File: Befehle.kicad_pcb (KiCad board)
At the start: 2 copper layers, 100 x 160 mm, 62 parts, among them J1 2PinTerminalBlocktg, J2 2PinTerminalBlocktg, J3 3PinTerminalBlocktg, J4 2PinTerminalBlocktg, J5 2PinTerminalBlocktg, P1 CONN_02X10, P2 CONN_02X10, U1 74LS14, U2 74540, U3 7400, U4 74HCT02, U5 74LS541, U6 74LS373, U7 74LS139, U8 74LS540

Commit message: Befehle: vor Umbau der Diodenmatrix im Schalplan
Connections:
- net Net-(P2-Pad2) renamed /AB0
- net Net-(P2-Pad3) renamed /AB1
- net Net-(P2-Pad4) renamed /AB2
- net Net-(P2-Pad5) renamed /AB3
- net Net-(P2-Pad6) renamed /AB4
- net Net-(P2-Pad7) renamed /AB5
- net Net-(P2-Pad8) renamed /AB6
- net Net-(P2-Pad9) renamed /AB7
- U1 pad 8: (no net) -> Net-(U1-Pad8)

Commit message: Befehle: Schaltplan bearbeitet
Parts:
- removed G***: LOGO, allBonsaiFootprintsLibs:agi5
- added C3: 100n, Capacitor_THT:C_Disc_D10.0mm_W2.5mm_P5.00mm, F.Cu at (129.0, 126.1)
- added C4: 100n, Capacitor_THT:C_Disc_D10.0mm_W2.5mm_P5.00mm, F.Cu at (129.0, 113.9)
- added C5: 100n, Capacitor_THT:C_Disc_D10.0mm_W2.5mm_P5.00mm, F.Cu at (129.0, 118.0)
- added C6: 100n, Capacitor_THT:C_Disc_D10.0mm_W2.5mm_P5.00mm, F.Cu at (140.6, 113.9)
- added C7: 100n, Capacitor_THT:C_Disc_D10.0mm_W2.5mm_P5.00mm, F.Cu at (129.0, 122.0)
- added C8: 100n, Capacitor_THT:C_Disc_D10.0mm_W2.5mm_P5.00mm, F.Cu at (140.6, 118.0)
- added C9: CP, Capacitor_THT:CP_Radial_D8.0mm_P2.50mm, F.Cu at (36.3, 11.1)
- added D23: bonsai_Led_Small_Platzhalter, bonsai:LED_Diodenmatrix_Platzhalter, F.Cu at (144.3, 121.8)
- added D24: bonsai_Led_Small_Platzhalter, bonsai:LED_Diodenmatrix_Platzhalter, F.Cu at (138.8, 125.5)
- added D25: bonsai_Led_Small_Platzhalter, bonsai:LED_Diodenmatrix_Platzhalter, F.Cu at (138.8, 121.8)
- added D26: bonsai_Led_Small_Platzhalter, bonsai:LED_Diodenmatrix_Platzhalter, F.Cu at (138.8, 129.1)
- added D27: bonsai_Led_Small_Platzhalter, bonsai:LED_Diodenmatrix_Platzhalter, F.Cu at (149.9, 123.3)
- added D28: bonsai_Led_Small_Platzhalter, bonsai:LED_Diodenmatrix_Platzhalter, F.Cu at (144.3, 125.5)
- added D29: bonsai_Led_Small_Platzhalter, bonsai:LED_Diodenmatrix_Platzhalter, F.Cu at (144.3, 129.1)
- added D30: bonsai_Led_Small_Platzhalter, bonsai:LED_Diodenmatrix_Platzhalter, F.Cu at (149.9, 126.9)
- added D31: bonsai_Led_Small_Platzhalter, bonsai:LED_Diodenmatrix_Platzhalter, F.Cu at (155.4, 123.3)
- added D32: bonsai_Led_Small_Platzhalter, bonsai:LED_Diodenmatrix_Platzhalter, F.Cu at (155.4, 126.9)
- C1, C2: footprint Capacitors_ThroughHole:C_Disc_D10.0mm_W2.5mm_P5.00mm -> Capacitor_THT:C_Disc_D10.0mm_W2.5mm_P5.00mm
- D11, D12, D15, D16, D19, D20: footprint allBonsaiFootprintsLibs:Diode_D1.8mm_W3.3mm_H2.4mmBonsai -> bonsai:LED_Diodenmatrix
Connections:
- D11 pad 1: 3 -> Net-(D11-Pad1)
- D11 pad 2: Net-(D11-Pad2) -> 3
- D12 pad 1: 3 -> Net-(D12-Pad1)
- D12 pad 2: Net-(D12-Pad2) -> 3
- D15 pad 1: 2 -> Net-(D11-Pad1)
- D15 pad 2: Net-(D11-Pad2) -> 2
- D16 pad 1: 2 -> Net-(D16-Pad1)
- D16 pad 2: Net-(D16-Pad2) -> 2
- D19 pad 1: 1 -> Net-(D19-Pad1)
- D19 pad 2: Net-(D19-Pad2) -> 1
- D20 pad 1: 0 -> Net-(D19-Pad1)
- D20 pad 2: Net-(D19-Pad2) -> 0
- U2 pad 1: GND -> Net-(U2-Pad1)
- U7 pad 4: Net-(D11-Pad2) -> Net-(D11-Pad1)
- U7 pad 5: Net-(D12-Pad2) -> Net-(D12-Pad1)
- U7 pad 6: Net-(D16-Pad2) -> Net-(D16-Pad1)
- U7 pad 7: Net-(D19-Pad2) -> Net-(D19-Pad1)
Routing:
- net Net-(D19-Pad2): track 47.8 -> 0.00 mm, vias 2 -> 0
- net Net-(D19-Pad1): track 0.00 -> 47.8 mm, vias 0 -> 2
- net Net-(D16-Pad2): track 46.1 -> 0.00 mm, vias 2 -> 0
- net Net-(D16-Pad1): track 0.00 -> 46.1 mm, vias 0 -> 2
- net Net-(D12-Pad2): track 42.4 -> 0.00 mm, vias 2 -> 0
- net Net-(D12-Pad1): track 0.00 -> 42.4 mm, vias 0 -> 2
- net Net-(D11-Pad2): track 38.2 -> 0.00 mm, vias 2 -> 0
- net Net-(D11-Pad1): track 0.00 -> 38.2 mm, vias 0 -> 2

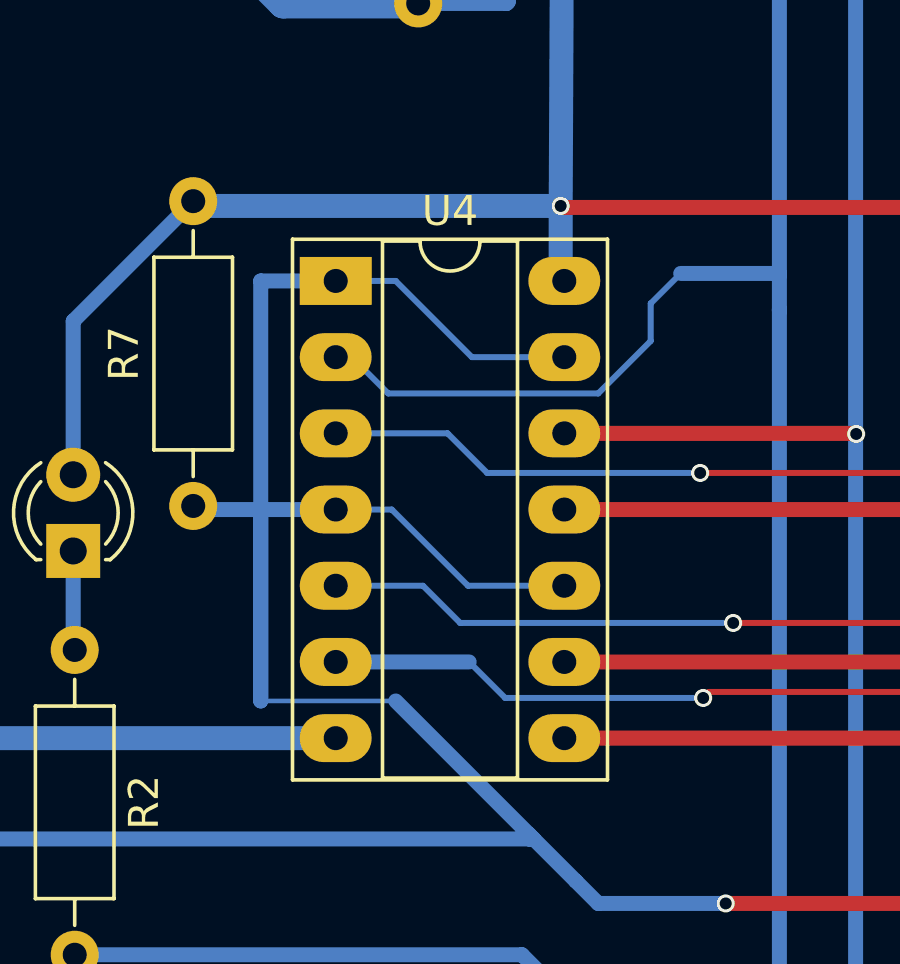
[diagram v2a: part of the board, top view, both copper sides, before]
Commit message: Befehle: Schaltplan geändert
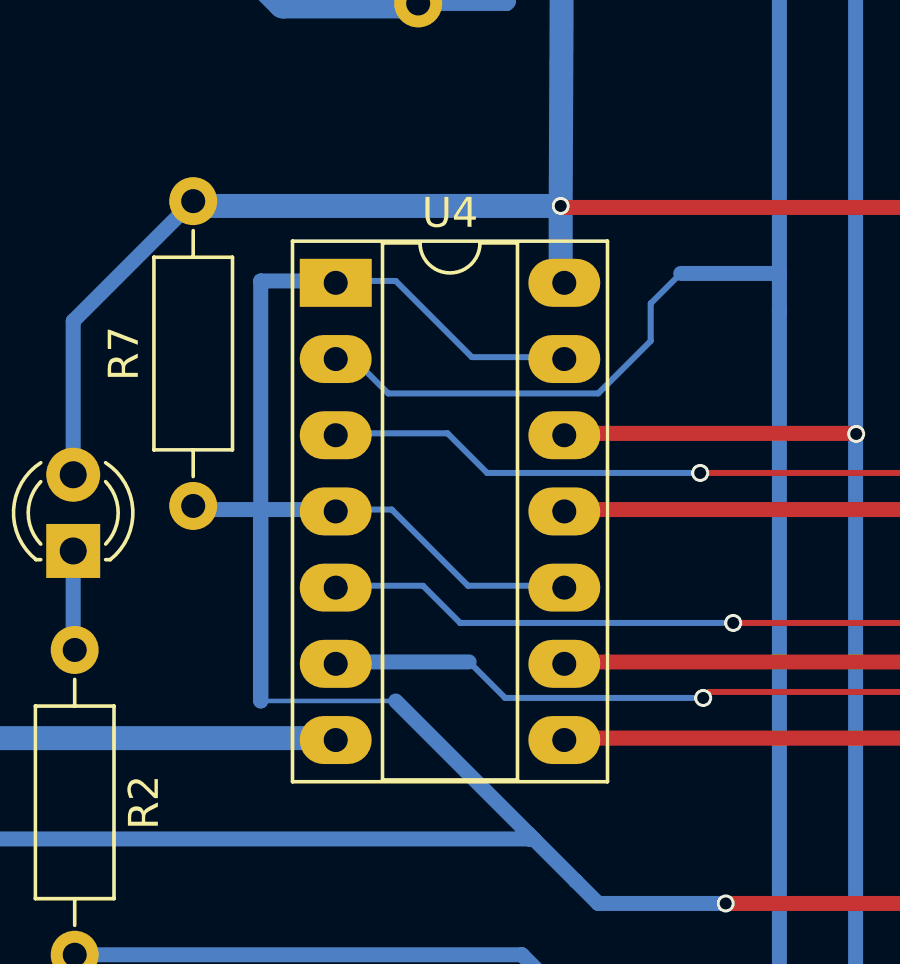
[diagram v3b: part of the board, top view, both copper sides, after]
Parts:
- U4: footprint allBonsaiFootprintsLibs:DIP-14_W7.62mm_Socket_LongPadstg -> Package_DIP:DIP-14_W7.62mm_Socket_LongPads
- moved U4 0.06 mm to (33.8, 117.1)
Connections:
- P2 pad 2: /AB0 -> /AB7
- P2 pad 3: /AB1 -> /AB6
- P2 pad 4: /AB2 -> /AB5
- P2 pad 5: /AB3 -> /AB4
- P2 pad 6: /AB4 -> /AB3
- P2 pad 7: /AB5 -> /AB2
- P2 pad 8: /AB6 -> /AB1
- P2 pad 9: /AB7 -> /AB0
- U2 pad 1: Net-(U2-Pad1) -> GND
- U5 pad 11: /AB0 -> /AB7
- U5 pad 12: /AB1 -> /AB6
- U5 pad 13: /AB2 -> /AB5
- U5 pad 14: /AB3 -> /AB4
- U5 pad 15: /AB4 -> /AB3
- U5 pad 16: /AB5 -> /AB2
- U5 pad 17: /AB6 -> /AB1
- U5 pad 18: /AB7 -> /AB0
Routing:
- net /AB7: track 34.0 -> 61.4 mm
- net /AB0: track 61.4 -> 34.0 mm
- net /AB6: track 37.3 -> 58.0 mm
- net /AB1: track 58.0 -> 37.3 mm
- net /AB5: track 41.2 -> 53.3 mm
- net /AB2: track 53.3 -> 41.2 mm
- net /AB4: track 45.1 -> 48.9 mm
- net /AB3: track 48.9 -> 45.1 mm

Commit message: Steuerwerk und Befehle bearbeitet
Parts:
- removed the C1 at (76.0, 60.0)
- removed the D17 at (99.0, 164.8)
- removed the D19 at (98.9, 125.4)
- removed the D30 at (149.9, 126.9)
- removed the D31 at (155.4, 123.3)
- removed the D32 at (155.4, 126.9)
- removed the D4 at (89.0, 164.8)
- removed the D7 at (94.0, 164.8)
- removed P1, P2: CONN_02X10, allBonsaiFootprintsLibs:Pin_Header_Straight_2x10_Pitch2.00mmBonsai.pretty
- removed the REF** at (116.3, 180.1)
- removed the U5 at (46.0, 67.0)
- added C10: 100n, Capacitor_THT:C_Disc_D10.0mm_W2.5mm_P5.00mm, F.Cu at (23.6, 66.4)
- added C2: 100n, Capacitor_THT:C_Disc_D10.0mm_W2.5mm_P5.00mm, F.Cu at (45.2, 58.8)
- added D11: bonsai_Led_Small_Platzhalter, bonsai:LED_Diodenmatrix_Platzhalter, F.Cu at (139.9, 137.5)
- added D13: Led_Small, bonsai:LED_Diodenmatrix, F.Cu at (132.3, 141.3)
- added D14: bonsai_Led_Small_Platzhalter, bonsai:LED_Diodenmatrix_Platzhalter, F.Cu at (136.1, 141.3)
- added D15: bonsai_Led_Small_Platzhalter, bonsai:LED_Diodenmatrix_Platzhalter, F.Cu at (139.9, 141.3)
- added D16: bonsai_Led_Small_Platzhalter, bonsai:LED_Diodenmatrix_Platzhalter, F.Cu at (143.7, 141.3)
- added D18: bonsai_Led_Small_Platzhalter, bonsai:LED_Diodenmatrix_Platzhalter, F.Cu at (132.3, 145.1)
- added D22: bonsai_Led_Small_Platzhalter, bonsai:LED_Diodenmatrix_Platzhalter, F.Cu at (132.3, 148.9)
- added J6: Conn_01x03, Connector_Molex:Molex_KK-254_AE-6410-03A_1x03_P2.54mm_Vertical, F.Cu at (2.33, 76.9)
- added REF**: EuroBoard160mmX100mm_holes_keepout, bonsai:EuroBoard160mmX100mm_holes_keepout, F.Cu at (114.2, 182.4)
- added U2: 74LS541, Package_DIP:DIP-20_W7.62mm_LongPads, F.Cu at (49.0, 65.1)
- added U8: 7408, Package_DIP:DIP-14_W7.62mm_Socket_LongPads, F.Cu at (21.7, 124.2)
- D1: renamed from D5; footprint LEDs:LED_D3.0mm -> LED_THT:LED_D3.0mm
- D12, D20: value Led_Small -> bonsai_Led_Small_Platzhalter; footprint bonsai:LED_Diodenmatrix -> bonsai:LED_Diodenmatrix_Platzhalter
- D17: renamed from D2; footprint LEDs:LED_D3.0mm -> LED_THT:LED_D3.0mm
- D2: renamed from D6; footprint LEDs:LED_D3.0mm -> LED_THT:LED_D3.0mm
- D21: value LED -> bonsai_Led_Small_Platzhalter; footprint LEDs:LED_D3.0mm -> bonsai:LED_Diodenmatrix_Platzhalter
- D24, D25: value bonsai_Led_Small_Platzhalter -> Led_Small; footprint bonsai:LED_Diodenmatrix_Platzhalter -> bonsai:LED_Diodenmatrix
- D26, D27, D28, D29: value bonsai_Led_Small_Platzhalter -> LED; footprint bonsai:LED_Diodenmatrix_Platzhalter -> LED_THT:LED_D3.0mm
- D3: renamed from D8; footprint LEDs:LED_D3.0mm -> LED_THT:LED_D3.0mm
- D30: renamed from D3; footprint LEDs:LED_D3.0mm -> LED_THT:LED_D3.0mm
- D31: renamed from D1; footprint LEDs:LED_D3.0mm -> LED_THT:LED_D3.0mm
- D32: renamed from D22; footprint Diodes_ThroughHole:D_DO-41_SOD81_P10.16mm_Horizontal -> Diode_THT:D_A-405_P10.16mm_Horizontal
- D4: renamed from D9; footprint LEDs:LED_D3.0mm -> LED_THT:LED_D3.0mm
- D5: renamed from D10; footprint LEDs:LED_D3.0mm -> LED_THT:LED_D3.0mm
- D6: renamed from D13; footprint LEDs:LED_D3.0mm -> LED_THT:LED_D3.0mm
- D7: renamed from D14; footprint LEDs:LED_D3.0mm -> LED_THT:LED_D3.0mm
- D8: renamed from D18; footprint LEDs:LED_D3.0mm -> LED_THT:LED_D3.0mm
- J1, J4: value 2PinTerminalBlocktg -> Conn_02x10_Odd_Even; footprint 2PinTerminalBlocktg -> Connector_PinHeader_2.54mm:PinHeader_2x10_P2.54mm_Vertical
- J2, J5: value 2PinTerminalBlocktg -> Conn_01x02; footprint 2PinTerminalBlocktg -> Connector_Molex:Molex_KK-254_AE-6410-02A_1x02_P2.54mm_Vertical
- J3: value 3PinTerminalBlocktg -> Conn_01x04; footprint 3PinTerminalBlocktg -> Connector_Molex:Molex_KK-254_AE-6410-04A_1x04_P2.54mm_Vertical
- R1: renamed from R10; footprint Resistors_ThroughHole:R_Axial_DIN0207_L6.3mm_D2.5mm_P10.16mm_Horizontal -> Resistor_THT:R_Axial_DIN0207_L6.3mm_D2.5mm_P10.16mm_Horizontal
- R10: renamed from R5; footprint Resistors_ThroughHole:R_Axial_DIN0207_L6.3mm_D2.5mm_P10.16mm_Horizontal -> Resistor_THT:R_Axial_DIN0207_L6.3mm_D2.5mm_P10.16mm_Horizontal
- R11: renamed from R4; footprint Resistors_ThroughHole:R_Axial_DIN0207_L6.3mm_D2.5mm_P10.16mm_Horizontal -> Resistor_THT:R_Axial_DIN0207_L6.3mm_D2.5mm_P10.16mm_Horizontal
- R12: renamed from R9; footprint Resistors_ThroughHole:R_Axial_DIN0207_L6.3mm_D2.5mm_P10.16mm_Horizontal -> Resistor_THT:R_Axial_DIN0207_L6.3mm_D2.5mm_P10.16mm_Horizontal
- R13: renamed from R12; footprint Resistors_ThroughHole:R_Axial_DIN0207_L6.3mm_D2.5mm_P10.16mm_Horizontal -> Resistor_THT:R_Axial_DIN0207_L6.3mm_D2.5mm_P10.16mm_Horizontal
- R14: renamed from R20; footprint Resistors_ThroughHole:R_Axial_DIN0207_L6.3mm_D2.5mm_P10.16mm_Horizontal -> Resistor_THT:R_Axial_DIN0207_L6.3mm_D2.5mm_P10.16mm_Horizontal
- R15: renamed from R24; footprint Resistors_ThroughHole:R_Axial_DIN0207_L6.3mm_D2.5mm_P10.16mm_Horizontal -> Resistor_THT:R_Axial_DIN0207_L6.3mm_D2.5mm_P10.16mm_Horizontal
- R16: renamed from R8; footprint Resistors_ThroughHole:R_Axial_DIN0207_L6.3mm_D2.5mm_P10.16mm_Horizontal -> Resistor_THT:R_Axial_DIN0207_L6.3mm_D2.5mm_P10.16mm_Horizontal
- R17: renamed from R2; footprint Resistors_ThroughHole:R_Axial_DIN0207_L6.3mm_D2.5mm_P10.16mm_Horizontal -> Resistor_THT:R_Axial_DIN0207_L6.3mm_D2.5mm_P10.16mm_Horizontal
- R18: renamed from R3; footprint Resistors_ThroughHole:R_Axial_DIN0207_L6.3mm_D2.5mm_P10.16mm_Horizontal -> Resistor_THT:R_Axial_DIN0207_L6.3mm_D2.5mm_P10.16mm_Horizontal
- R19: renamed from R6; footprint Resistors_ThroughHole:R_Axial_DIN0207_L6.3mm_D2.5mm_P10.16mm_Horizontal -> Resistor_THT:R_Axial_DIN0207_L6.3mm_D2.5mm_P10.16mm_Horizontal
- R2: renamed from R11; footprint Resistors_ThroughHole:R_Axial_DIN0207_L6.3mm_D2.5mm_P10.16mm_Horizontal -> Resistor_THT:R_Axial_DIN0207_L6.3mm_D2.5mm_P10.16mm_Horizontal
- R3: renamed from R13; footprint Resistors_ThroughHole:R_Axial_DIN0207_L6.3mm_D2.5mm_P10.16mm_Horizontal -> Resistor_THT:R_Axial_DIN0207_L6.3mm_D2.5mm_P10.16mm_Horizontal
- R4: renamed from R14; footprint Resistors_ThroughHole:R_Axial_DIN0207_L6.3mm_D2.5mm_P10.16mm_Horizontal -> Resistor_THT:R_Axial_DIN0207_L6.3mm_D2.5mm_P10.16mm_Horizontal
- R5: renamed from R15; footprint Resistors_ThroughHole:R_Axial_DIN0207_L6.3mm_D2.5mm_P10.16mm_Horizontal -> Resistor_THT:R_Axial_DIN0207_L6.3mm_D2.5mm_P10.16mm_Horizontal
- R6: renamed from R16; footprint Resistors_ThroughHole:R_Axial_DIN0207_L6.3mm_D2.5mm_P10.16mm_Horizontal -> Resistor_THT:R_Axial_DIN0207_L6.3mm_D2.5mm_P10.16mm_Horizontal
- R7: renamed from R18; footprint Resistors_ThroughHole:R_Axial_DIN0207_L6.3mm_D2.5mm_P10.16mm_Horizontal -> Resistor_THT:R_Axial_DIN0207_L6.3mm_D2.5mm_P10.16mm_Horizontal
- R8: renamed from R21; footprint Resistors_ThroughHole:R_Axial_DIN0207_L6.3mm_D2.5mm_P10.16mm_Horizontal -> Resistor_THT:R_Axial_DIN0207_L6.3mm_D2.5mm_P10.16mm_Horizontal
- R9: renamed from R1; footprint Resistors_ThroughHole:R_Axial_DIN0207_L6.3mm_D2.5mm_P10.16mm_Horizontal -> Resistor_THT:R_Axial_DIN0207_L6.3mm_D2.5mm_P10.16mm_Horizontal
- RP1: footprint Resistors_ThroughHole:R_Array_SIP5 -> Resistor_THT:R_Array_SIP5
- U1: footprint allBonsaiFootprintsLibs:DIP-14_W7.62mm_Socket_LongPadstg -> Package_DIP:DIP-14_W7.62mm_Socket_LongPads
- U3: renamed from U8; footprint allBonsaiFootprintsLibs:DIP-20_W7.62mm_Socket_LongPadstg -> Package_DIP:DIP-20_W7.62mm_LongPads
- U4: renamed from U7; footprint allBonsaiFootprintsLibs:DIP-16_W7.62mm_Socket_LongPadstg -> Package_DIP:DIP-16_W7.62mm_Socket_LongPads
- U5: renamed from U6; footprint allBonsaiFootprintsLibs:DIP-20_W7.62mm_Socket_LongPadstg -> Package_DIP:DIP-20_W7.62mm_LongPads
- U6: renamed from U2; footprint allBonsaiFootprintsLibs:DIP-20_W7.62mm_Socket_LongPadstg -> Package_DIP:DIP-20_W7.62mm_LongPads
- U7: renamed from U4; value 74HCT02 -> 7402
- U9: renamed from U3; footprint allBonsaiFootprintsLibs:DIP-14_W7.62mm_Socket_LongPadstg -> Package_DIP:DIP-14_W7.62mm_Socket_LongPads
- moved J5 159.5 mm to (34.3, 25.2), turned to 0 degrees
- moved C8 106.1 mm to (23.0, 120.4)
- moved C9 104.8 mm to (39.5, 145.8)
- moved C7 101.3 mm to (39.5, 120.4)
- moved C5 87.9 mm to (42.6, 97.5), turned to 270 degrees
- moved J3 77.7 mm to (100.8, 174.6), turned to 180 degrees
- moved D27 69.6 mm to (94.0, 164.8), turned to 270 degrees
- moved D26 61.3 mm to (89.0, 164.8), turned to 270 degrees
- moved D28 60.0 mm to (99.0, 164.8), turned to 270 degrees
- moved C6 55.3 mm to (79.5, 142.6), turned to 90 degrees
- moved D29 53.7 mm to (104.2, 164.8), turned to 270 degrees
- moved D12 52.7 mm to (143.7, 137.5), turned to 45 degrees
- moved C4 49.3 mm to (88.4, 98.1), turned to 270 degrees
- moved D19 45.5 mm to (136.1, 145.1), turned to 45 degrees
- moved D10 44.7 mm to (136.1, 137.5), turned to 45 degrees
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- renumbered C9 to C1, C2 to C3, C3 to C4, C4 to C5, C5 to C6, C6 to C7, C7 to C8, C8 to C9, D15 to D10, D16 to D19, D11 to D9
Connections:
- D10 pad 1: Net-(D11-Pad1) -> /h0
- D10 pad 2: 2 -> /v2
- D12 pad 1: Net-(D12-Pad1) -> /h0
- D12 pad 2: 3 -> /v0
- D19 pad 1: Net-(D16-Pad1) -> /h2
- D19 pad 2: 2 -> /v2
- D20 pad 1: Net-(D19-Pad1) -> /h2
- D20 pad 2: 0 -> /v1
- D21 pad 1: Net-(D21-Pad1) -> /h2
- D21 pad 2: VCC -> /v0
- D23 pad 1: 3 -> /h3
- D23 pad 2: Net-(D16-Pad1) -> /v2
- D24 pad 1: 1 -> /h3
- D24 pad 2: Net-(D11-Pad1) -> /v1
- D25 pad 1: 0 -> /h3
- D25 pad 2: Net-(D11-Pad1) -> /v0
- D26 pad 1: 2 -> Net-(D26-Pad1)
- D26 pad 2: Net-(D12-Pad1) -> VCC
- D27 pad 1: 1 -> Net-(D27-Pad1)
- D27 pad 2: Net-(D12-Pad1) -> VCC
- D28 pad 1: 0 -> Net-(D28-Pad1)
- D28 pad 2: Net-(D12-Pad1) -> VCC
- D29 pad 1: 1 -> Net-(D29-Pad1)
- D29 pad 2: Net-(D16-Pad1) -> VCC
- D9 pad 1: Net-(D11-Pad1) -> /h0
- D9 pad 2: 3 -> /v3
- J1 pad 2: VCC -> GND
- J3 pad 1: upPC -> /v0
- J3 pad 2: incPCz -> /v1
- J3 pad 3: incPC -> /v2
- J4 pad 1: 0 -> GND
- J4 pad 2: 1 -> GND
- J5 pad 1: 2 -> GND
- J5 pad 2: 3 -> VCC
- R12 pad 1: Net-(D4-Pad1) (its old number) -> Net-(D26-Pad1)
- R13 pad 1: Net-(D7-Pad1) (its old number) -> Net-(D27-Pad1)
- R14 pad 1: Net-(D17-Pad1) (its old number) -> Net-(D28-Pad1)
- R15 pad 1: Net-(D21-Pad1) -> Net-(D29-Pad1)
- R18 pad 1: incPCz -> ~incPCz
- R19 pad 1: incPC -> ~incPC
- R7 pad 1: Net-(R18-Pad1) -> Net-(R7-Pad1)
- RP1 pad 2: 0 -> /v0
- RP1 pad 3: 1 -> /v1
- RP1 pad 4: 2 -> /v2
- RP1 pad 5: 3 -> /v3
- U3 pad 12: Net-(R18-Pad1) -> Net-(R7-Pad1)
- U3 pad 2: /a4 -> /a7
- U3 pad 3: /a7 -> /a6
- U3 pad 4: /a6 -> /a5
- U3 pad 5: /a5 -> /a4
- U3 pad 6: /a8 -> /a3
- U3 pad 7: /a3 -> /a2
- U3 pad 8: /a2 -> /a1
- U3 pad 9: /a1 -> /a0
- U4 pad 2: /a7 -> /b0
- U4 pad 3: /a4 -> /b1
- U4 pad 4: Net-(D11-Pad1) -> /h0
- U4 pad 5: Net-(D12-Pad1) -> /h1
- U4 pad 6: Net-(D16-Pad1) -> /h2
- U4 pad 7: Net-(D19-Pad1) -> /h3
- U5 pad 13: /d4 -> /DB4
- U5 pad 14: /d5 -> /DB5
- U5 pad 15: /a6 -> /a5
- U5 pad 16: /a8 -> /b0
- U5 pad 17: /d3 -> /DB6
- U5 pad 18: /d1 -> /DB7
- U5 pad 19: /a2 -> /b1
- U5 pad 2: /a1 -> /a0
- U5 pad 3: /d2 -> /DB0
- U5 pad 4: /d7 -> /DB1
- U5 pad 5: /a3 -> /a1
- U5 pad 6: /a5 -> /a2
- U5 pad 7: /d44 -> /DB2
- U5 pad 8: /d6 -> /DB3
- U5 pad 9: /a7 -> /a3
- U6 pad 2: 0 -> /v0
- U6 pad 3: 1 -> /v1
- U6 pad 4: 2 -> /v2
- U6 pad 5: 3 -> /v3
- U6 pad 9: Net-(R7-Pad1) -> /is0
- U7 pad 1: Net-(R7-Pad1) -> Net-(U7-Pad1)
- U7 pad 10: Net-(R7-Pad1) -> Net-(U7-Pad10)
- U7 pad 11: /d3 -> /DB6
- U7 pad 12: /d1 -> /DB7
- U7 pad 13: Net-(R7-Pad1) -> Net-(U7-Pad13)
- U7 pad 2: /d2 -> /DB0
- U7 pad 3: /d7 -> /DB1
- U7 pad 4: Net-(R7-Pad1) -> Net-(U7-Pad4)
- U7 pad 5: /d44 -> /DB2
- U7 pad 6: /d6 -> /DB3
- U7 pad 8: /d4 -> /DB4
- U7 pad 9: /d5 -> /DB5
- U9 pad 1: Net-(R7-Pad1) -> /is0
- U9 pad 10: Net-(U3-Pad10) -> (no net)
- U9 pad 11: upPC -> (no net)
- U9 pad 12: Net-(U3-Pad12) -> (no net)
- U9 pad 13: Net-(U3-Pad12) -> (no net)
- U9 pad 14: VCC -> Vcc
- U9 pad 2: Net-(U3-Pad2) -> incPCz
- U9 pad 3: Net-(U3-Pad10) -> /~is0_&_incPCz
- U9 pad 4: incPCz -> ~incPCz
- U9 pad 5: incPCz -> ~incPCz
- U9 pad 6: Net-(U3-Pad2) -> incPCz
- U9 pad 8: Net-(U3-Pad12) -> (no net)
- U9 pad 9: incPC -> (no net)
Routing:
- net GND: track 690.1 -> 0.00 mm, vias 4 -> 0
- net VCC: track 710.2 -> 35.1 mm, vias 8 -> 0
- net Net-(R7-Pad1): track 143.8 -> 0.00 mm, vias 2 -> 0
- net /a1: track 104.0 -> 0.00 mm, vias 2 -> 0
- net /a7: track 103.5 -> 0.00 mm, vias 2 -> 0
- net /d4: track 102.2 -> 0.00 mm, vias 1 -> 0
- net loadIR: track 100.2 -> 0.00 mm, vias 2 -> 0
- net /d6: track 97.7 -> 0.00 mm, vias 2 -> 0
- net /d5: track 95.8 -> 0.00 mm, vias 1 -> 0
- net /d44: track 94.5 -> 0.00 mm, vias 2 -> 0
- net /d3: track 91.7 -> 0.00 mm, vias 1 -> 0
- net /a3: track 91.1 -> 0.00 mm, vias 2 -> 0
- net /a2: track 89.6 -> 0.00 mm, vias 2 -> 0
- net /d7: track 88.6 -> 0.00 mm, vias 2 -> 0
- net /d2: track 86.0 -> 0.00 mm
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
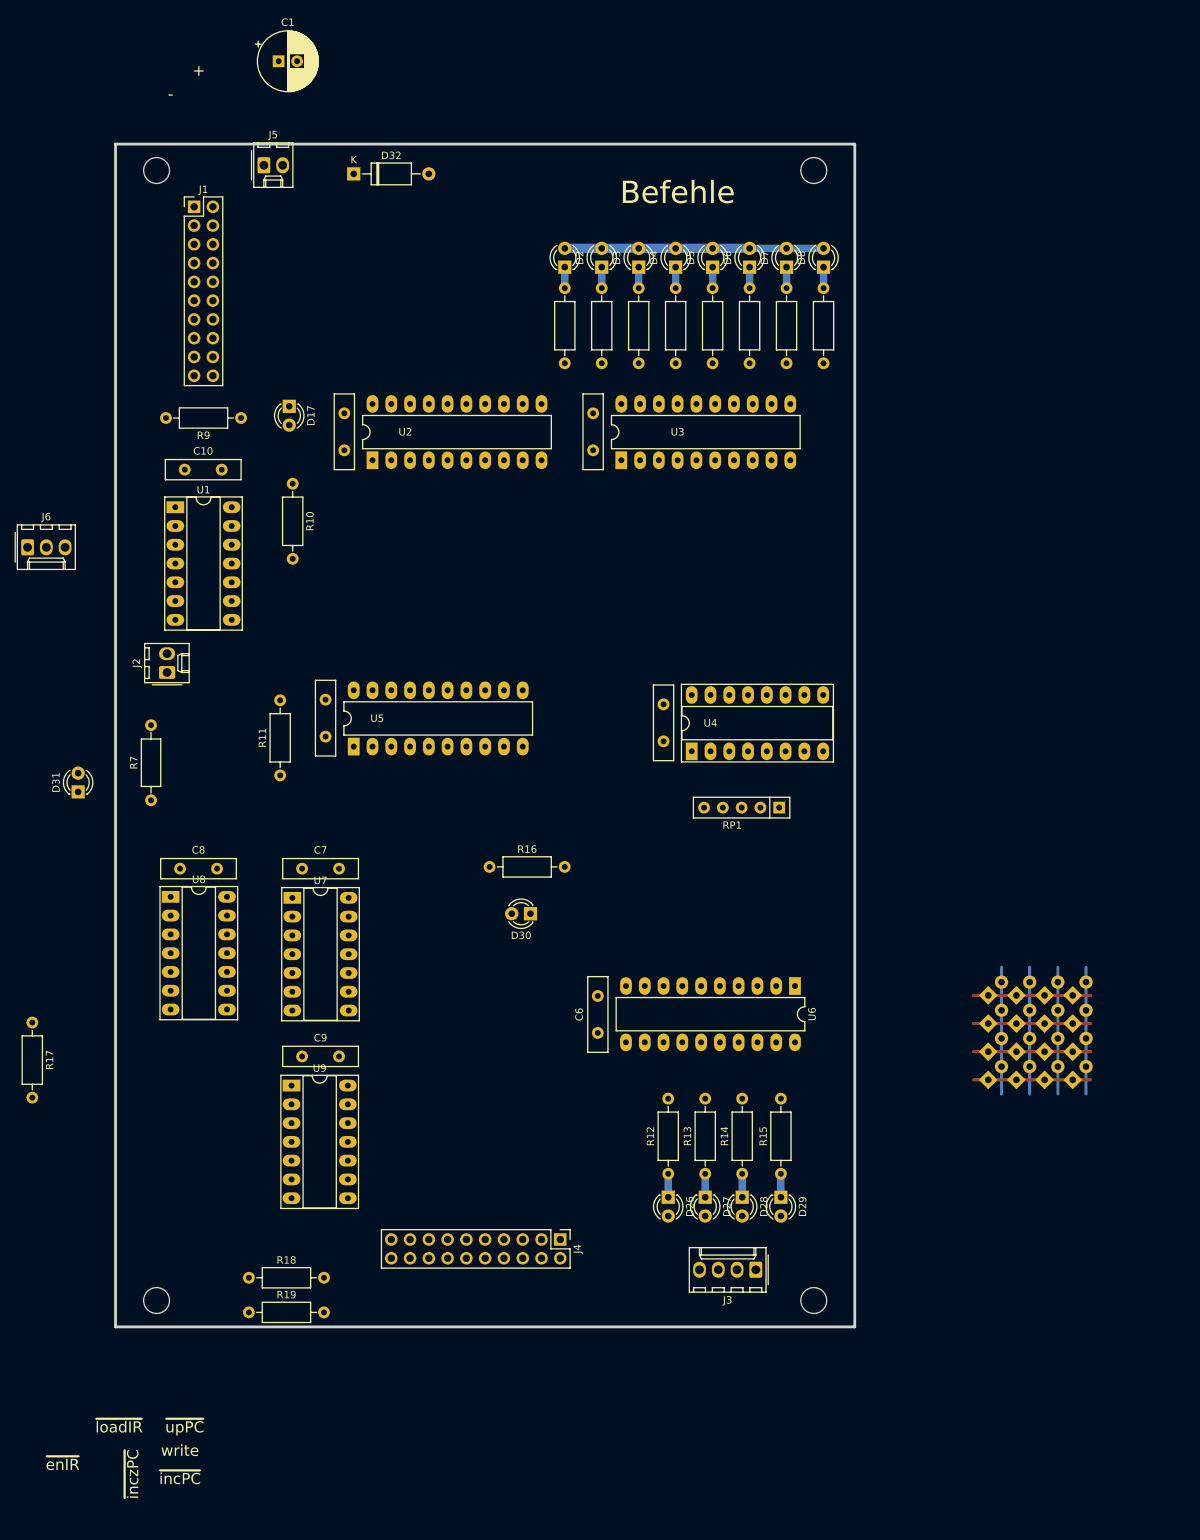
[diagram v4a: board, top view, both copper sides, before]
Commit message: Footprint EuroBoard gedreht und auf das Gitter gelegt (Ursprung links oben)
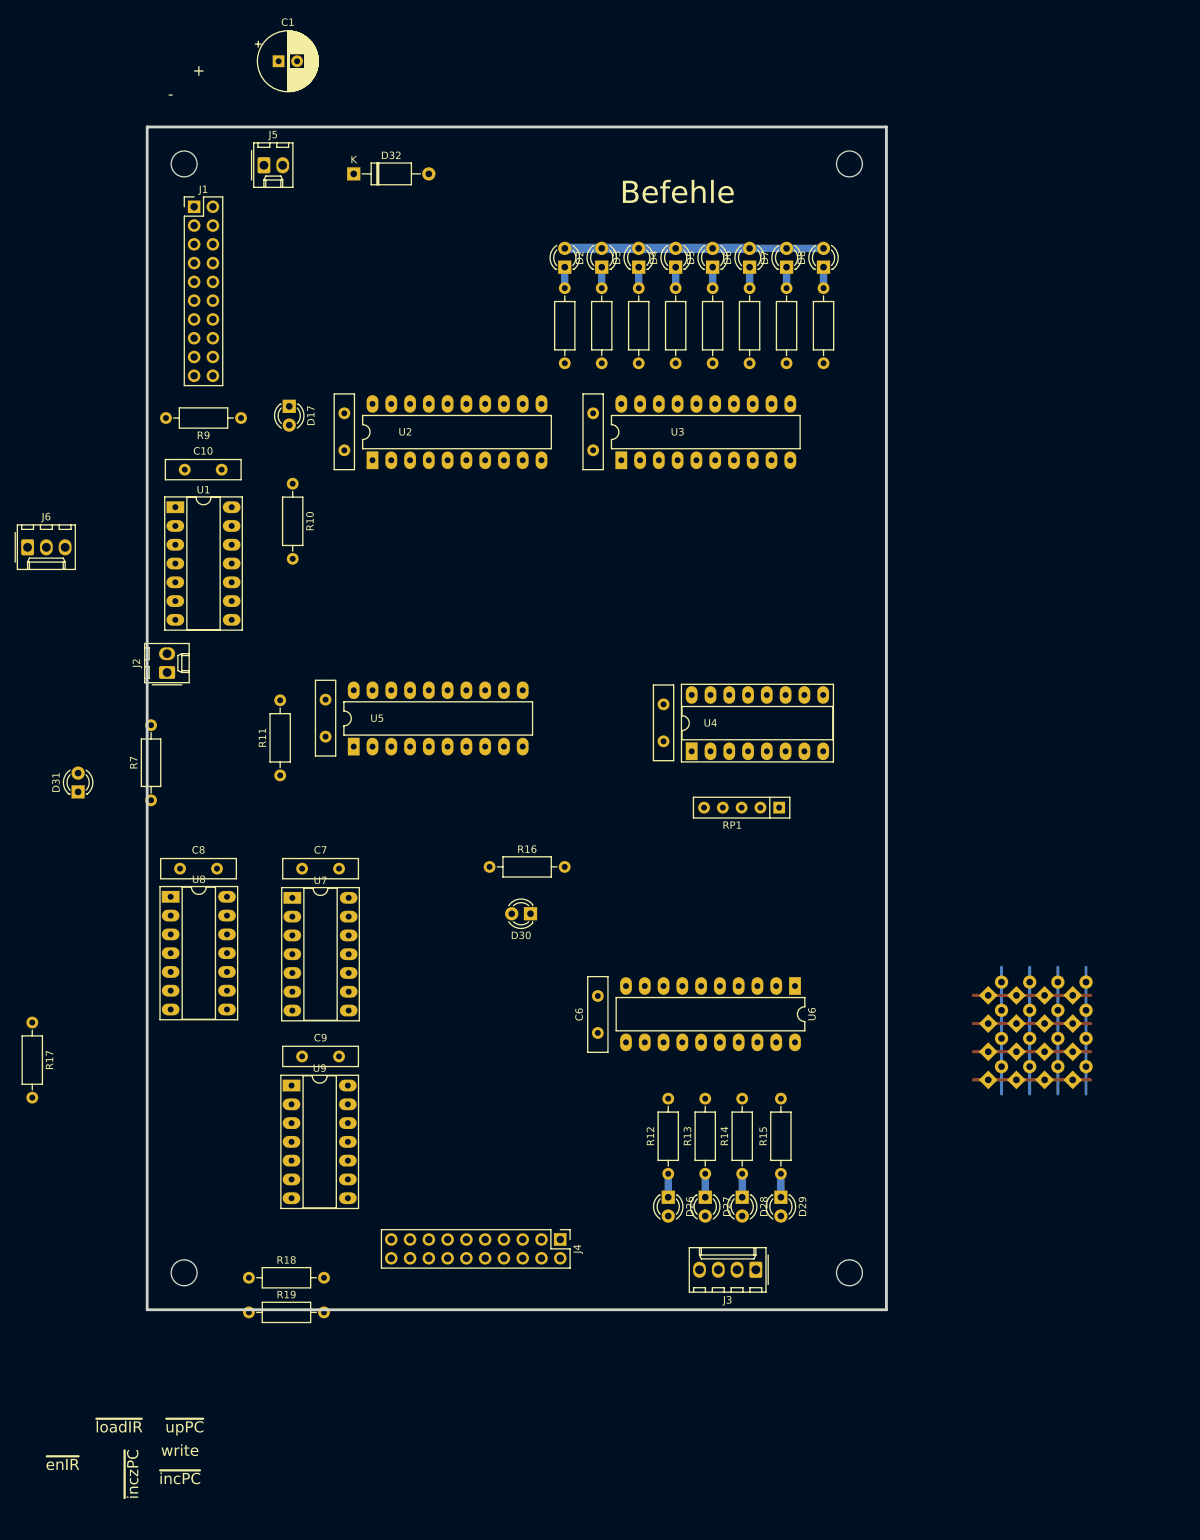
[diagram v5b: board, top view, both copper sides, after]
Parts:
- moved REF** 188.4 mm to (18.5, 20.0), turned to 0 degrees
